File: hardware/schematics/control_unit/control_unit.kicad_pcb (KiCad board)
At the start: 2 copper layers, 151.3 x 95.4 mm, 134 parts, among them J1 Screw_Terminal_01x12, J2 Screw_Terminal_01x08, J3 Screw_Terminal_01x08, J4 AudioJack4, J5 Screw_Terminal_01x08, J6 6P6C, J7 Conn_01x03_Pin, J8 Conn_01x03_Pin, K1 Relay_SPDT, K2 Relay_SPDT, K3 Relay_SPDT, K4 Relay_SPDT, Q1 2N7000, Q10 IRFZ44N, Q11 IRFZ44N, Q12 IRFZ44N, Q13 IRFZ44N, Q14 IRFZ44N, Q15 IRFZ44N, Q16 IRFZ44N, Q17 IRFZ44N, Q18 2N7000, Q2 2N7000, Q3 IRFZ44N, Q4 IRFZ44N, Q5 IRFZ44N, Q6 2N7000, Q7 2N7000, Q8 IRFZ44N, Q9 IRFZ44N, T1 Transformer_1P_1S, U1 PC817, U10 PC817, U11 PC817, U12 PC817, U13 PC817, U14 MAX487E, U15 ESP-WROOM-32, U16 LM2596T-ADJ, U17 LM35-D, U18 LM324, U2 PC817, U3 PC817, U4 PC817, U5 PC817, U6 PC817, U7 PC817, U8 PC817, U9 PC817

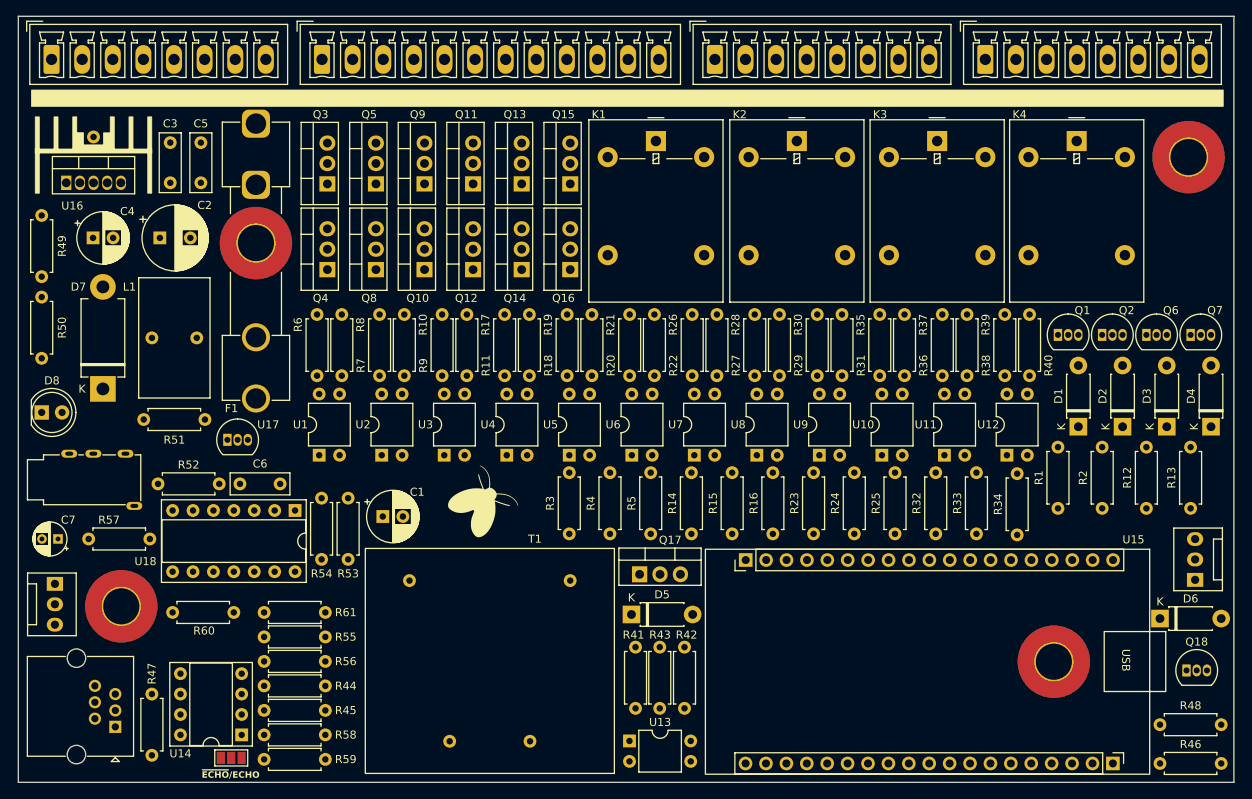
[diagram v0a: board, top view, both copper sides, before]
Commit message: feat: final PCB topological design.
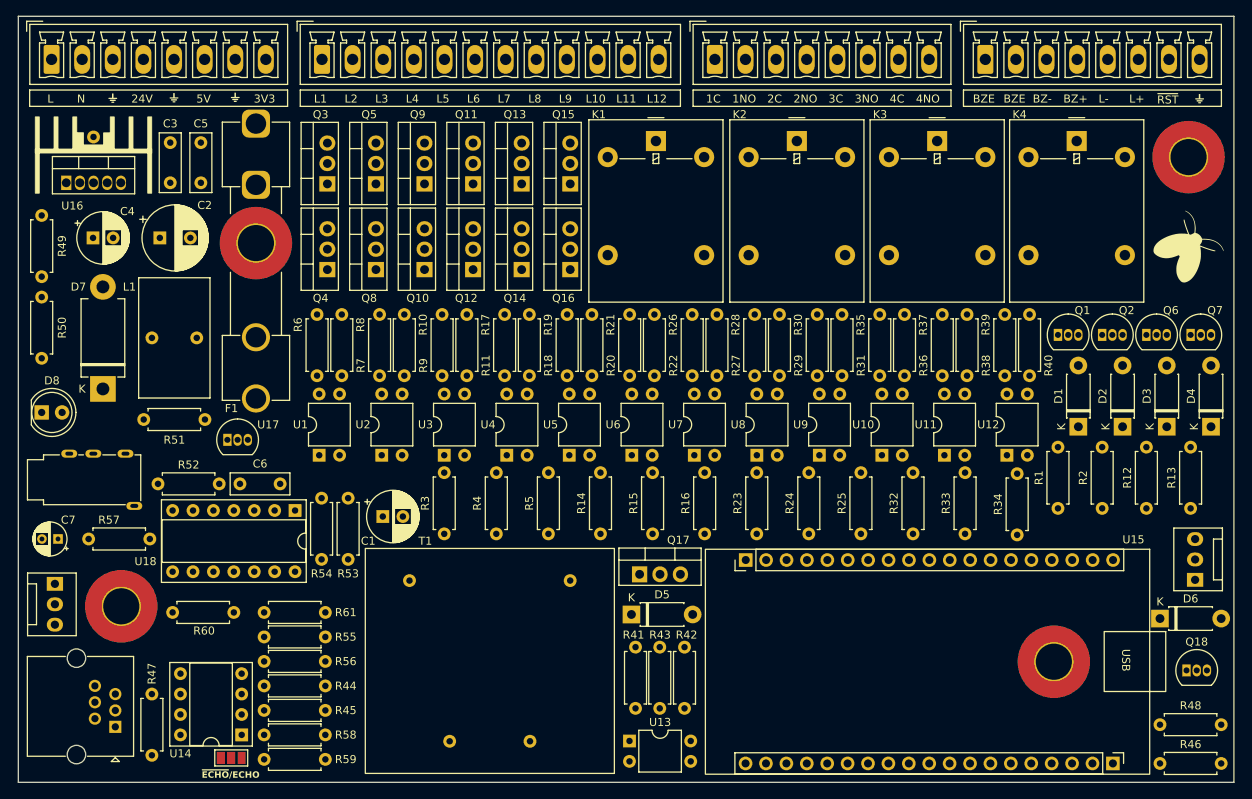
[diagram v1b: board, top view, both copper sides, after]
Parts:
- added G***: LOGO, LOGO, F.Cu at (86.6, 61.5)
- added G***: LOGO, LOGO, F.Cu at (101.8, 61.4)
- added G***: LOGO, LOGO, F.Cu at (221.8, 61.5)
- added G***: LOGO, LOGO, F.Cu at (94.2, 61.4)
- moved G*** 93.4 mm to (220.1, 80.3)
- moved R3 15.6 mm to (127.8, 115.7)
- moved R4 14.1 mm to (134.3, 115.7)
- moved R5 12.7 mm to (140.8, 115.7)
- moved R14 11.3 mm to (147.3, 115.7)
- moved R15 9.90 mm to (153.8, 115.7)
- moved R16 8.49 mm to (160.2, 115.7)
- moved R23 7.07 mm to (166.7, 115.7)
- moved R24 5.66 mm to (173.2, 115.7)
- moved R25 4.24 mm to (179.7, 115.7)
- moved R32 2.83 mm to (186.2, 115.7)
- moved R33 1.41 mm to (192.7, 115.7)
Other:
- board text added: "1C"
- board text added: "1NO"
- board text added: "24V"
- board text added: "2C"
- board text added: "2NO"
- board text added: "3C"
- board text added: "3NO"
- board text added: "3V3"
- board text added: "4C"
- board text added: "4NO"
- board text added: "5V"
- board text added: "BZ+"
- board text added: "BZ-"
- board text added: "BZE"
- board text added: "L"
- board text added: "L+"
- board text added: "L-"
- board text added: "L1"
- board text added: "L10"
- board text added: "L11"
- board text added: "L12"
- board text added: "L2"
- board text added: "L3"
- board text added: "L4"
- board text added: "L5"
- board text added: "L6"
- board text added: "L7"
- board text added: "L8"
- board text added: "L9"
- board text added: "N"
- board text added: "~{RST}"

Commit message: !feat: control_unit first PCB release.
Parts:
- moved T1 41.8 mm to (118.0, 117.5), turned to 0 degrees
- moved D7 11.3 mm to (85.1, 86.4), turned to -90 degrees
- moved R3 2.54 mm to (130.4, 115.7)
- moved R4 2.31 mm to (136.6, 115.7)
- moved R5 2.08 mm to (142.9, 115.7)
- moved R14 1.85 mm to (149.1, 115.7)
- moved R15 1.62 mm to (155.4, 115.7)
- moved R16 1.39 mm to (161.6, 115.7)
- moved R23 1.15 mm to (167.9, 115.7)
- moved C1 1.02 mm to (121.2, 113.5)
- moved R24 0.92 mm to (174.1, 115.7)
- moved R25 0.69 mm to (180.4, 115.7)
- moved R32 0.46 mm to (186.6, 115.7)
- moved C4 0.25 mm to (84.4, 78.9)
- moved R46 0.25 mm to (216.7, 144.3)
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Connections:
- J5 pad 5: Net-(J5-Pin_3) -> GND
- J5 pad 7: Net-(J5-Pin_3) -> GND
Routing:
- net +5V: track 0.00 -> 438.9 mm, vias 0 -> 8
- net +24V: track 0.00 -> 322.4 mm, vias 0 -> 8
- net /PERIPHERALS/FAN-: track 0.00 -> 165.3 mm, vias 0 -> 14
- net /AC_L: track 0.00 -> 163.8 mm
- net /~{RESET}: track 0.00 -> 156.2 mm, vias 0 -> 3
- net +3.3V: track 0.00 -> 151.6 mm
- net /AC_N: track 0.00 -> 145.4 mm
- net /AC_I_IN_1: track 0.00 -> 117.3 mm, vias 0 -> 6
- net /MCU/DE/~{RE}: track 0.00 -> 114.7 mm, vias 0 -> 4
- net /PERIPHERALS/BUZZER_EN_2: track 0.00 -> 107.9 mm, vias 0 -> 4
- net /MCU/TX: track 0.00 -> 104.8 mm, vias 0 -> 4
- net /HOMEMONITOR/I: track 0.00 -> 97.8 mm, vias 0 -> 8
- net /PERIPHERALS/LED-: track 0.00 -> 97.8 mm, vias 0 -> 12
- net /MCU/TEMP: track 0.00 -> 93.4 mm, vias 0 -> 4
- net /MCU/O2: track 0.00 -> 91.0 mm, vias 0 -> 13
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- added copper zone on B.Cu, net GND
- added copper zone on F.Cu, net GND
- added copper zone on F.Cu, net Net-(J5-Pin_3)
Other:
- board size 151.3 x 95.4 mm -> 151.8 x 95.4 mm

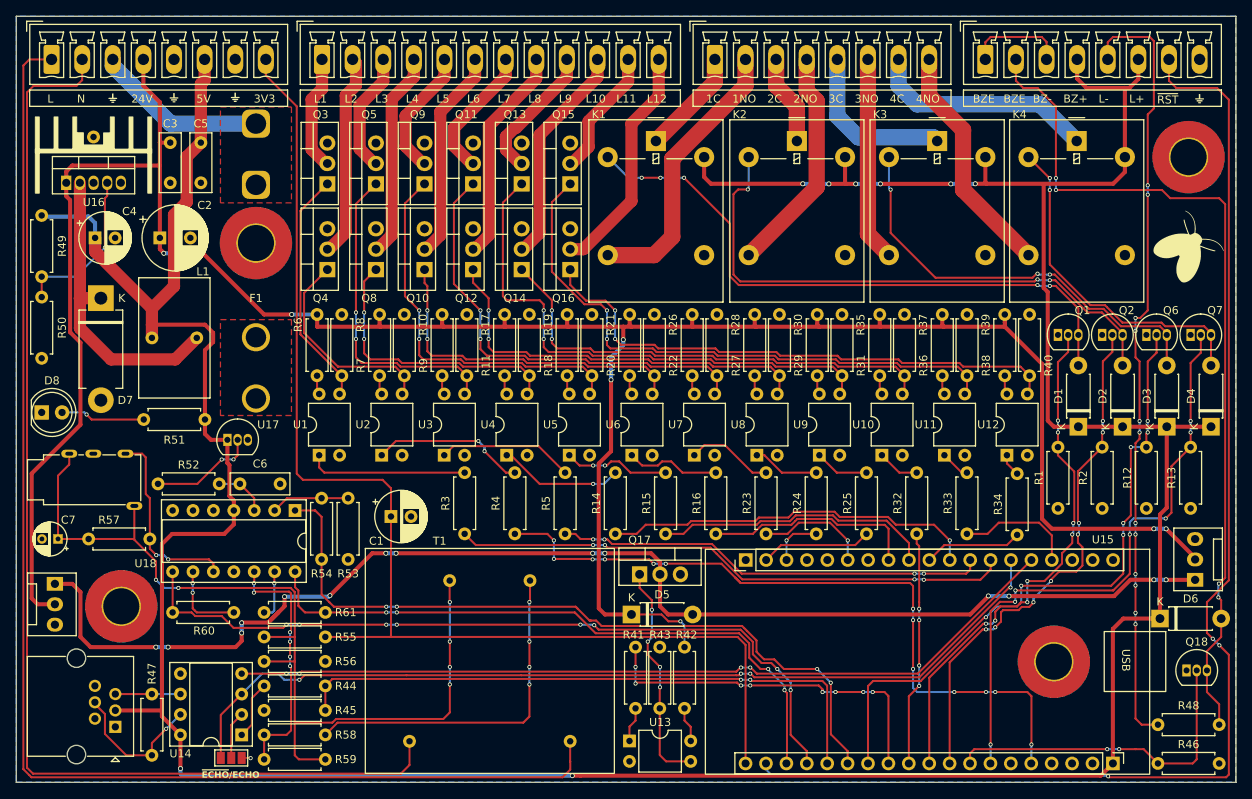
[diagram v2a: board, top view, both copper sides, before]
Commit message: chore: rotated silkscreens.
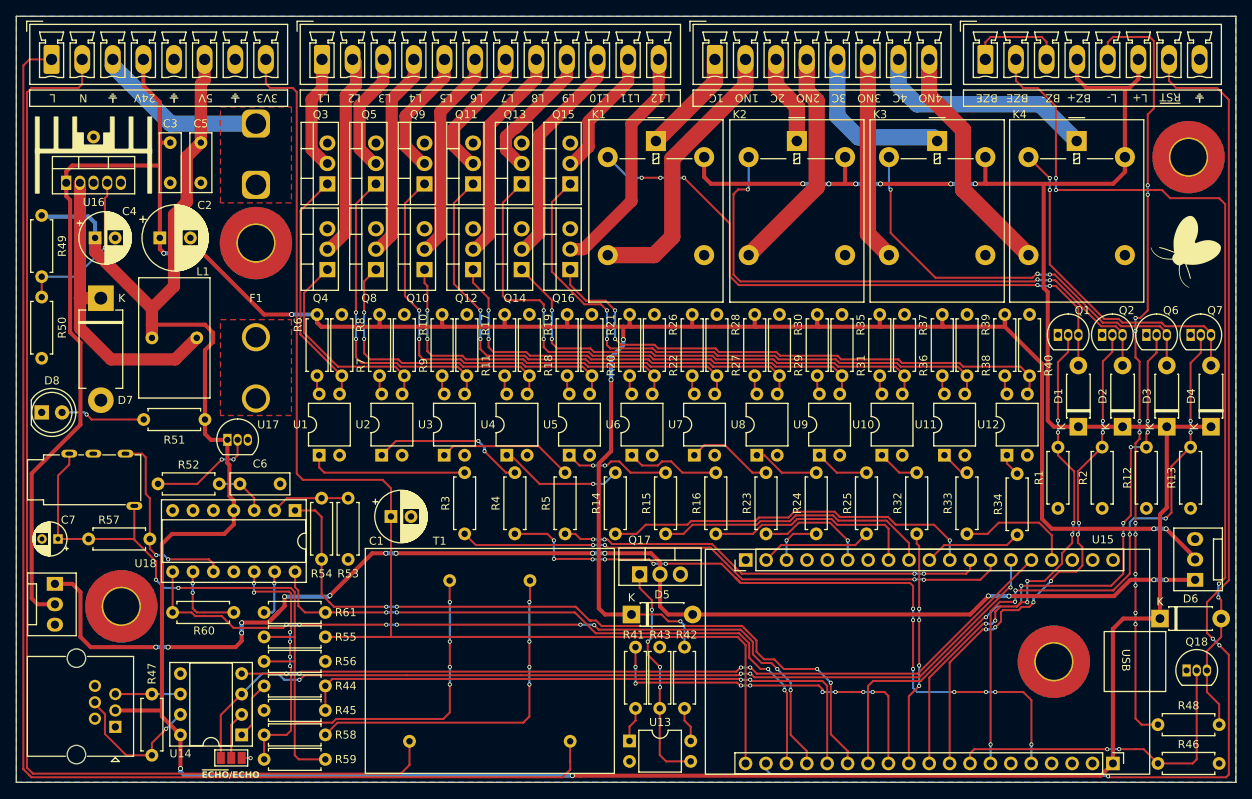
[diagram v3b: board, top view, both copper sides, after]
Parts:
- moved G*** 0.33 mm to (220.5, 80.3), turned to 180 degrees
- moved G*** 0.11 mm to (101.8, 61.5), turned to 180 degrees
- moved G*** 0.06 mm to (221.8, 61.5), turned to 180 degrees
- moved G*** 0.05 mm to (94.2, 61.5), turned to 180 degrees
- turned G*** to 180 degrees
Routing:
- net +3.3V: track 151.6 -> 153.3 mm

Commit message: feat: added PowerMonitor resistor's values.
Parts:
- R55, R56: value 10k -> 1k
- R57: value R -> 120
- R58: value R -> 10k
- R59: value R -> 820
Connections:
- net /HOMEMONITOR/I renamed /MCU/AC_I
- net /HOMEMONITOR/V renamed /MCU/AC_V
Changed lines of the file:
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@@
 	(net 104 "/MCU/TEMP")
 	(net 105 "Net-(U18D-+)")
-	(net 106 "/HOMEMONITOR/I")
+	(net 106 "/MCU/AC_I")
 	(net 107 "Net-(U18C--)")
 	(net 108 "Net-(U18D--)")
-	(net 109 "/HOMEMONITOR/V")
+	(net 109 "/MCU/AC_V")
 	(net 110 "/MCU/TX")
 	(net 111 "unconnected-(U15-RXD{slash}G3-Pad24)")
@@
 			)
 		)
-		(property "Value" "R"
+		(property "Value" "120"
 			(at 3.81 2.37 0)
 			(layer "F.Fab")
@@
 		)
 		(property ki_fp_filters "R_*")
-		(sheetname "HOMEMONITOR")
-		(sheetfile "untitled.kicad_sch")
+		(sheetname "POWERMONITOR")
+		(sheetfile "powermonitor.kicad_sch")
 		(attr through_hole)
 		(fp_line
@@
 		)
 		(property ki_fp_filters "CP_*")
-		(sheetname "HOMEMONITOR")
-		(sheetfile "untitled.kicad_sch")
+		(sheetname "POWERMONITOR")
+		(sheetfile "powermonitor.kicad_sch")
 		(attr through_hole)
 		(fp_line
@@
 		(at 86.57493 61.468 180)
 		(property "Reference" "G***"
-			(at 0 0 360)
+			(at 0 0 0)
 			(layer "F.SilkS")
 			(hide yes)
@@
 		)
 		(property "Value" "LOGO"
-			(at 0.75 0 360)
+			(at 0.75 0 0)
 			(layer "F.SilkS")
 			(hide yes)
@@
 		)
 		(property "Footprint" ""
-			(at 0 0 360)
+			(at 0 0 0)
 			(layer "F.Fab")
 			(hide yes)
@@
 		)
 		(property "Datasheet" ""
-			(at 0 0 360)
+			(at 0 0 0)
 			(layer "F.Fab")
 			(hide yes)
@@
 		)
 		(property "Description" ""
-			(at 0 0 360)
+			(at 0 0 0)
 			(layer "F.Fab")
 			(hide yes)
@@
 			(layers "*.Cu" "*.Mask")
 			(remove_unused_layers no)
-			(net 106 "/HOMEMONITOR/I")
+			(net 106 "/MCU/AC_I")
 			(pinfunction "SN/G39")
 			(pintype "bidirectional")
@@
 			(layers "*.Cu" "*.Mask")
 			(remove_unused_layers no)
-			(net 109 "/HOMEMONITOR/V")
+			(net 109 "/MCU/AC_V")
 			(pinfunction "SP/G36")
 			(pintype "bidirectional")
@@
 			)
 		)
-		(property "Value" "R"
+		(property "Value" "820"
 			(at 3.81 2.37 0)
 			(layer "F.Fab")
@@
 		)
 		(property ki_fp_filters "R_*")
-		(sheetname "HOMEMONITOR")
-		(sheetfile "untitled.kicad_sch")
+		(sheetname "POWERMONITOR")
+		(sheetfile "powermonitor.kicad_sch")
 		(attr through_hole)
 		(fp_line
@@
 		(at 220.472 80.264 180)
 		(property "Reference" "G***"
-			(at 0 0 360)
+			(at 0 0 0)
 			(layer "F.SilkS")
 			(hide yes)
@@
 		)
 		(property "Value" "LOGO"
-			(at 0.75 0 360)
+			(at 0.75 0 0)
 			(layer "F.SilkS")
 			(hide yes)
@@
 		)
 		(property "Footprint" ""
-			(at 0 0 360)
+			(at 0 0 0)
 			(layer "F.Fab")
 			(hide yes)
@@
 		)
 		(property "Datasheet" ""
-			(at 0 0 360)
+			(at 0 0 0)
 			(layer "F.Fab")
 			(hide yes)
@@
 		)
 		(property "Description" ""
-			(at 0 0 360)
+			(at 0 0 0)
 			(layer "F.Fab")
 			(hide yes)
@@
 		(at 101.81493 61.468 180)
 		(property "Reference" "G***"
-			(at 0 0 360)
+			(at 0 0 0)
 			(layer "F.SilkS")
 			(hide yes)
@@
 		)
 		(property "Value" "LOGO"
-			(at 0.75 0 360)
+			(at 0.75 0 0)
 			(layer "F.SilkS")
 			(hide yes)
@@
 		)
 		(property "Footprint" ""
-			(at 0 0 360)
+			(at 0 0 0)
 			(layer "F.Fab")
 			(hide yes)
@@
 		)
 		(property "Datasheet" ""
-			(at 0 0 360)
+			(at 0 0 0)
 			(layer "F.Fab")
 			(hide yes)
@@
 		)
 		(property "Description" ""
-			(at 0 0 360)
+			(at 0 0 0)
 			(layer "F.Fab")
 			(hide yes)
@@
 		)
 		(property ki_fp_filters "R_*")
-		(sheetname "HOMEMONITOR")
-		(sheetfile "untitled.kicad_sch")
+		(sheetname "POWERMONITOR")
+		(sheetfile "powermonitor.kicad_sch")
 		(attr through_hole)
 		(fp_line
@@
 			(layers "*.Cu" "*.Mask")
 			(remove_unused_layers no)
-			(net 109 "/HOMEMONITOR/V")
+			(net 109 "/MCU/AC_V")
 			(pintype "passive")
 		)
@@
 		(at 221.84743 61.468 180)
 		(property "Reference" "G***"
-			(at 0 0 360)
+			(at 0 0 0)
 			(layer "F.SilkS")
 			(hide yes)
@@
 		)
 		(property "Value" "LOGO"
-			(at 0.75 0 360)
+			(at 0.75 0 0)
 			(layer "F.SilkS")
 			(hide yes)
@@
 		)
 		(property "Footprint" ""
-			(at 0 0 360)
+			(at 0 0 0)
 			(layer "F.Fab")
 			(hide yes)
@@
 		)
 		(property "Datasheet" ""
-			(at 0 0 360)
+			(at 0 0 0)
 			(layer "F.Fab")
 			(hide yes)
@@
 		)
 		(property "Description" ""
-			(at 0 0 360)
+			(at 0 0 0)
 			(layer "F.Fab")
 			(hide yes)
@@
 		)
 		(property ki_fp_filters "R_*")
-		(sheetname "HOMEMONITOR")
-		(sheetfile "untitled.kicad_sch")
+		(sheetname "POWERMONITOR")
+		(sheetfile "powermonitor.kicad_sch")
 		(attr through_hole)
 		(fp_line
@@
 			(layers "*.Cu" "*.Mask")
 			(remove_unused_layers no)
-			(net 106 "/HOMEMONITOR/I")
+			(net 106 "/MCU/AC_I")
 			(pintype "passive")
 		)
@@
 		(at 94.19493 61.468 180)
 		(property "Reference" "G***"
-			(at 0 0 360)
+			(at 0 0 0)
 			(layer "F.SilkS")
 			(hide yes)
@@
 		)
 		(property "Value" "LOGO"
-			(at 0.75 0 360)
+			(at 0.75 0 0)
 			(layer "F.SilkS")
 			(hide yes)
@@
 		)
 		(property "Footprint" ""
-			(at 0 0 360)
+			(at 0 0 0)
 			(layer "F.Fab")
 			(hide yes)
@@
 		)
 		(property "Datasheet" ""
-			(at 0 0 360)
+			(at 0 0 0)
 			(layer "F.Fab")
 			(hide yes)
@@
 		)
 		(property "Description" ""
-			(at 0 0 360)
+			(at 0 0 0)
 			(layer "F.Fab")
 			(hide yes)
@@
 			(layers "*.Cu" "*.Mask")
 			(remove_unused_layers no)
-			(net 106 "/HOMEMONITOR/I")
+			(net 106 "/MCU/AC_I")
 			(pintype "output")
 		)
@@
 			(layers "*.Cu" "*.Mask")
 			(remove_unused_layers no)
-			(net 109 "/HOMEMONITOR/V")
+			(net 109 "/MCU/AC_V")
 			(pintype "output")
 		)
@@
 			)
 		)
-		(sheetname "HOMEMONITOR")
-		(sheetfile "untitled.kicad_sch")
+		(sheetname "POWERMONITOR")
+		(sheetfile "powermonitor.kicad_sch")
 		(attr through_hole)
 		(fp_rect
@@
 			)
 		)
-		(property "Value" "R"
+		(property "Value" "10k"
 			(at 3.81 2.37 0)
 			(layer "F.Fab")
@@
 		)
 		(property ki_fp_filters "R_*")
-		(sheetname "HOMEMONITOR")
-		(sheetfile "untitled.kicad_sch")
+		(sheetname "POWERMONITOR")
+		(sheetfile "powermonitor.kicad_sch")
 		(attr through_hole)
 		(fp_line
@@
 			)
 		)
-		(property "Value" "10k"
+		(property "Value" "1k"
 			(at 3.81 2.37 0)
 			(layer "F.Fab")
@@
 		)
 		(property ki_fp_filters "R_*")
-		(sheetname "HOMEMONITOR")
-		(sheetfile "untitled.kicad_sch")
+		(sheetname "POWERMONITOR")
+		(sheetfile "powermonitor.kicad_sch")
 		(attr through_hole)
 		(fp_line
@@
 			)
 		)
-		(property "Value" "10k"
+		(property "Value" "1k"
 			(at 3.81 2.37 0)
 			(layer "F.Fab")
@@
 		)
 		(property ki_fp_filters "R_*")
-		(sheetname "HOMEMONITOR")
-		(sheetfile "untitled.kicad_sch")
+		(sheetname "POWERMONITOR")
+		(sheetfile "powermonitor.kicad_sch")
 		(attr through_hole)
 		(fp_line
